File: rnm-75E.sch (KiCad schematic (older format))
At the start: 12 parts

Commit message: new crystal
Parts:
- removed C?: 1uF, symbol Device:C_Small
- removed C? (x3): 0.1uF, symbol Device:C_Small
- removed C?: 10uF, symbol Device:C_Small
- removed C? (x2): 22pF, symbol Device:C_Small
- removed R?: 10k, symbol Device:R_Small
- removed R? (x2): 22, symbol Device:R_Small
- removed U?: ATmega32U4-AU, Package_QFP:TQFP-44_10x10mm_P0.8mm, symbol MCU_Microchip_ATmega:ATmega32U4-AU
- removed Y?: 16MHz, symbol Device:Crystal_GND24_Small
- added C?: 1uF, symbol Device:C_Small
- added C? (x3): 0.1uF, symbol Device:C_Small
- added C?: 10uF, symbol Device:C_Small
- added C? (x2): 22pF, symbol Device:C_Small
- added R?: 10k, symbol Device:R_Small
- added U?: ATmega32U4-AU, Package_QFP:TQFP-44_10x10mm_P0.8mm, symbol MCU_Microchip_ATmega:ATmega32U4-AU
- added Y?: MHz, symbol Device:Crystal_GND24_Small
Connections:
- wire segments 37 -> 38

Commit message: mcu complete?
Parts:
- added R?: 10k, symbol Device:R_Small
- added R? (x2): 22k, symbol Device:R_Small
- added SW?: SW_Push, symbol Switch:SW_Push
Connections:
- net +5V: now also R?.1
- net GND: now also SW?.1
- net at U?.13 (~RESET): now also R?.2, SW?.2
- net at U?.3 (D-): now also R?.1
- net at U?.4 (D+): now also R?.1
- new net D+: R?.2
- new net D-: R?.2
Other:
- moved on the sheet: R?
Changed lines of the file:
@@
 L Device:R_Small R?
 U 1 1 609AD2BE
-P 4750 3600
-F 0 "R?" V 4554 3600 50  0000 C CNN
-F 1 "10k" V 4645 3600 50  0000 C CNN
-F 2 "" H 4750 3600 50  0001 C CNN
-F 3 "~" H 4750 3600 50  0001 C CNN
-	1    4750 3600
+P 4350 3600
+F 0 "R?" V 4154 3600 50  0000 C CNN
+F 1 "10k" V 4245 3600 50  0000 C CNN
+F 2 "" H 4350 3600 50  0001 C CNN
+F 3 "~" H 4350 3600 50  0001 C CNN
+	1    4350 3600
 	0    1    1    0
 $EndComp
@@
 L power:GND #PWR?
 U 1 1 609AEDAA
-P 5250 3600
-F 0 "#PWR?" H 5250 3350 50  0001 C CNN
-F 1 "GND" H 5255 3427 50  0000 C CNN
-F 2 "" H 5250 3600 50  0001 C CNN
-F 3 "" H 5250 3600 50  0001 C CNN
-	1    5250 3600
-	1    0    0    -1
-$EndComp
-Wire Wire Line
-	4150 3600 4650 3600
-Wire Wire Line
-	4850 3600 5250 3600
+P 4650 3600
+F 0 "#PWR?" H 4650 3350 50  0001 C CNN
+F 1 "GND" H 4655 3427 50  0000 C CNN
+F 2 "" H 4650 3600 50  0001 C CNN
+F 3 "" H 4650 3600 50  0001 C CNN
+	1    4650 3600
+	1    0    0    -1
+$EndComp
+Wire Wire Line
+	4150 3600 4250 3600
 $Comp
 L Device:C_Small C?
@@
 L power:+5V #PWR?
 U 1 1 609B8BFA
-P 1250 2300
-F 0 "#PWR?" H 1250 2150 50  0001 C CNN
-F 1 "+5V" H 1265 2473 50  0000 C CNN
-F 2 "" H 1250 2300 50  0001 C CNN
-F 3 "" H 1250 2300 50  0001 C CNN
-	1    1250 2300
-	1    0    0    -1
-$EndComp
-Wire Wire Line
-	1250 2300 2950 2300
+P 2200 2300
+F 0 "#PWR?" H 2200 2150 50  0001 C CNN
+F 1 "+5V" H 2215 2473 50  0000 C CNN
+F 2 "" H 2200 2300 50  0001 C CNN
+F 3 "" H 2200 2300 50  0001 C CNN
+	1    2200 2300
+	1    0    0    -1
+$EndComp
 $Comp
 L Device:Crystal_GND24_Small Y?
@@
 Wire Wire Line
 	2100 2000 2100 1800
+$Comp
+L Switch:SW_Push SW?
+U 1 1 609C5DAF
+P 2500 1500
+F 0 "SW?" H 2500 1785 50  0000 C CNN
+F 1 "SW_Push" H 2500 1694 50  0000 C CNN
+F 2 "" H 2500 1700 50  0001 C CNN
+F 3 "~" H 2500 1700 50  0001 C CNN
+	1    2500 1500
+	1    0    0    -1
+$EndComp
+$Comp
+L power:GND #PWR?
+U 1 1 609C76B8
+P 1700 1350
+F 0 "#PWR?" H 1700 1100 50  0001 C CNN
+F 1 "GND" H 1705 1177 50  0000 C CNN
+F 2 "" H 1700 1350 50  0001 C CNN
+F 3 "" H 1700 1350 50  0001 C CNN
+	1    1700 1350
+	1    0    0    -1
+$EndComp
+Wire Wire Line
+	1700 1350 1700 1250
+Wire Wire Line
+	1700 1250 2150 1250
+Wire Wire Line
+	2150 1250 2150 1500
+Wire Wire Line
+	2150 1500 2300 1500
+Wire Wire Line
+	2700 1500 2800 1500
+$Comp
+L Device:R_Small R?
+U 1 1 609CB514
+P 2800 1300
+F 0 "R?" H 2859 1346 50  0000 L CNN
+F 1 "10k" H 2859 1255 50  0000 L CNN
+F 2 "" H 2800 1300 50  0001 C CNN
+F 3 "~" H 2800 1300 50  0001 C CNN
+	1    2800 1300
+	1    0    0    -1
+$EndComp
+$Comp
+L power:+5V #PWR?
+U 1 1 609CC955
+P 2800 1100
+F 0 "#PWR?" H 2800 950 50  0001 C CNN
+F 1 "+5V" H 2815 1273 50  0000 C CNN
+F 2 "" H 2800 1100 50  0001 C CNN
+F 3 "" H 2800 1100 50  0001 C CNN
+	1    2800 1100
+	1    0    0    -1
+$EndComp
+Connection ~ 2800 1500
+Wire Wire Line
+	2800 1500 2950 1500
+Wire Wire Line
+	2800 1400 2800 1500
+Wire Wire Line
+	2800 1200 2800 1100
+Text GLabel 1400 2500 0    50   Input ~ 0
+D+
+Text GLabel 1400 2600 0    50   Input ~ 0
+D-
+Wire Wire Line
+	2950 2500 1850 2500
+$Comp
+L Device:R_Small R?
+U 1 1 609D1BD5
+P 1750 2500
+F 0 "R?" V 1554 2500 50  0000 C CNN
+F 1 "22k" V 1645 2500 50  0000 C CNN
+F 2 "" H 1750 2500 50  0001 C CNN
+F 3 "~" H 1750 2500 50  0001 C CNN
+	1    1750 2500
+	0    1    1    0
+$EndComp
+Wire Wire Line
+	1650 2500 1400 2500
+Wire Wire Line
+	1400 2600 1900 2600
+$Comp
+L Device:R_Small R?
+U 1 1 609D369C
+P 2000 2600
+F 0 "R?" V 1804 2600 50  0000 C CNN
+F 1 "22k" V 1895 2600 50  0000 C CNN
+F 2 "" H 2000 2600 50  0001 C CNN
+F 3 "~" H 2000 2600 50  0001 C CNN
+	1    2000 2600
+	0    1    1    0
+$EndComp
+Wire Wire Line
+	2100 2600 2950 2600
+Wire Wire Line
+	2200 2300 2950 2300
+Wire Wire Line
+	4450 3600 4650 3600
 $EndSCHEMATC

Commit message: ref made
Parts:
- added D1, D2, D3, D4: D_Small, Diode_SMD:D_SOD-123, symbol Device:D_Small
- added F1: Polyfuse, Fuse:Fuse_1206_3216Metric, symbol Device:Polyfuse
- added MX1, MX2, MX3, MX4: MX-NoLED, MX_ALPS:MX-1U-NoLED, symbol MX_ALPS:MX-NoLED
- added USB1: Molex-0548190519, random_keyboard_parts:Molex-0548190589, symbol random_keyb_parts:Molex-0548190519
- C1, C2, C3, C4, C5, C6: renamed from C?; footprint (none) -> Capacitor_SMD:C_0805_2012Metric
- C7: renamed from C?; footprint (none) -> Diode_SMD:D_SOD-123
- R1, R2, R3, R4: renamed from R?; footprint (none) -> Resistor_SMD:R_0805_2012Metric
- SW1: renamed from SW?; footprint (none) -> random_keyboard_parts:SKQG-1155865
- Y1: renamed from Y?; footprint (none) -> Package_QFP:TQFP-44_10x10mm_P0.8mm
- gave numbers to parts that had none: 1
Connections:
- net +5V: now also F1.1
- net D+: now also USB1.3 (D+)
- net D-: now also USB1.4 (D-)
- net GND: now also USB1.1 (GND)
- net ROW0: now reaches U1.27 (PD7)
- net ROW0: now also D1.1 (K), D3.1 (K)
- net COL1: now reaches U1.28 (PB4)
- net COL1: now also MX3.1 (COL), MX4.1 (COL)
- net COL0: now reaches U1.29 (PB5)
- net COL0: now also MX1.1 (COL), MX2.1 (COL)
- net ROW1: now reaches U1.30 (PB6)
- net ROW1: now also D2.1 (K), D4.1 (K)
- new net: D1.2 (A), MX1.2 (ROW)
- new net: D3.2 (A), MX3.2 (ROW)
- new net: D2.2 (A), MX2.2 (ROW)
- new net: D4.2 (A), MX4.2 (ROW)
- new net VCC: F1.2, USB1.5 (VBUS)
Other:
- moved on the sheet: R4

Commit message: added ground fill
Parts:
- added C8: 0.1uF, Capacitor_SMD:C_0805_2012Metric, symbol Device:C_Small
- Y1: value MHz -> Crystal_GND24_Small; footprint Package_QFP:TQFP-44_10x10mm_P0.8mm -> Crystal:Crystal_SMD_3225-4Pin_3.2x2.5mm
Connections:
- net +5V: now also C8.1
- net GND: now also C8.2
- net ROW1: now also U1.26 (PD6); no longer U1.30 (PB6)
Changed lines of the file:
@@
 $EndComp
-$Comp
-L Device:Crystal_GND24_Small Y1
-U 1 1 609BC559
-P 2250 1800
-F 0 "Y1" V 2204 1944 50  0000 L CNN
-F 1 "MHz" V 2295 1944 50  0000 L CNN
-F 2 "Package_QFP:TQFP-44_10x10mm_P0.8mm" H 2250 1800 50  0001 C CNN
-F 3 "~" H 2250 1800 50  0001 C CNN
-	1    2250 1800
-	0    1    1    0
-$EndComp
-Wire Wire Line
-	2250 1700 2950 1700
-Wire Wire Line
-	2950 1900 2250 1900
 $Comp
 L Device:C_Small C4
@@
 	2050 1950 2050 1900
 Wire Wire Line
-	2050 1900 2250 1900
-Connection ~ 2250 1900
-Wire Wire Line
 	2050 1600 2050 1700
-Wire Wire Line
-	2050 1700 2250 1700
-Connection ~ 2250 1700
 Wire Wire Line
 	1850 1600 1850 1950
@@
 Wire Wire Line
 	4150 3600 4400 3600
-Text GLabel 4150 2100 2    50   Input ~ 0
+Text GLabel 4150 3300 2    50   Input ~ 0
 ROW1
 Text GLabel 4150 2000 2    50   Input ~ 0
@@
 Text GLabel 4150 1900 2    50   Input ~ 0
 COL1
+$Comp
+L Device:Crystal_GND24_Small Y1
+U 1 1 609B4FA0
+P 2250 1800
+F 0 "Y1" V 2204 1944 50  0000 L CNN
+F 1 "Crystal_GND24_Small" V 2295 1944 50  0000 L CNN
+F 2 "Crystal:Crystal_SMD_3225-4Pin_3.2x2.5mm" H 2250 1800 50  0001 C CNN
+F 3 "~" H 2250 1800 50  0001 C CNN
+	1    2250 1800
+	0    1    1    0
+$EndComp
+Wire Wire Line
+	2050 1700 2250 1700
+Wire Wire Line
+	2050 1900 2250 1900
+Connection ~ 2250 1700
+Wire Wire Line
+	2250 1700 2950 1700
+Connection ~ 2250 1900
+Wire Wire Line
+	2250 1900 2950 1900
+$Comp
+L Device:C_Small C8
+U 1 1 60A5117E
+P 550 4200
+F 0 "C8" H 642 4246 50  0000 L CNN
+F 1 "0.1uF" H 642 4155 50  0000 L CNN
+F 2 "Capacitor_SMD:C_0805_2012Metric" H 550 4200 50  0001 C CNN
+F 3 "~" H 550 4200 50  0001 C CNN
+	1    550  4200
+	1    0    0    -1
+$EndComp
+Wire Wire Line
+	550  4300 850  4300
+Connection ~ 850  4300
+Wire Wire Line
+	850  4100 550  4100
+Connection ~ 850  4100
 $EndSCHEMATC

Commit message: keyboard schematic done
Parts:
- removed C1, C2, C3, C8: 0.1uF, Capacitor_SMD:C_0805_2012Metric, symbol Device:C_Small
- removed C4, C5: 22pF, Capacitor_SMD:C_0805_2012Metric, symbol Device:C_Small
- removed C6: 10uF, Capacitor_SMD:C_0805_2012Metric, symbol Device:C_Small
- removed C7: 1uF, Diode_SMD:D_SOD-123, symbol Device:C_Small
- removed D1, D2, D3, D4: D_Small, Diode_SMD:D_SOD-123, symbol Device:D_Small
- removed F1: Polyfuse, Fuse:Fuse_1206_3216Metric, symbol Device:Polyfuse
- removed MX1, MX2, MX3, MX4: MX-NoLED, MX_ALPS:MX-1U-NoLED, symbol MX_ALPS:MX-NoLED
- removed R1, R2: 22k, Resistor_SMD:R_0805_2012Metric, symbol Device:R_Small
- removed R3, R4: 10k, Resistor_SMD:R_0805_2012Metric, symbol Device:R_Small
- removed SW1: SW_Push, random_keyboard_parts:SKQG-1155865, symbol Switch:SW_Push
- removed U1: ATmega32U4-AU, Package_QFP:TQFP-44_10x10mm_P0.8mm, symbol MCU_Microchip_ATmega:ATmega32U4-AU
- removed USB1: Molex-0548190519, random_keyboard_parts:Molex-0548190589, symbol random_keyb_parts:Molex-0548190519
- removed Y1: Crystal_GND24_Small, Crystal:Crystal_SMD_3225-4Pin_3.2x2.5mm, symbol Device:Crystal_GND24_Small
- added CF3, C_F1, C_F2, C_F4: 0.1uF, symbol Device:C_Small
- added C_FM: 10uF, symbol Device:C_Small
- added C_X1, C_X2: 22pF, symbol Device:C_Small
- added C_ucap: 1uF, symbol Device:C_Small
- added D? (x87): D_Small, symbol Device:D_Small
- added ESD?: PRTR5V0U2X, Package_TO_SOT_SMD:SOT-143, symbol Power_Protection:PRTR5V0U2X
- added F1: 500mA, symbol Device:Polyfuse_Small
- added J?: USB_C_Receptacle_USB2.0, symbol Connector:USB_C_Receptacle_USB2.0
- added J?: AVR-ISP-6, symbol Connector:AVR-ISP-6
- added MX? (x89): MX-NoLED, symbol MX_ALPS_HYBRID:MX-NoLED
- added R_SW1, R_SW2: 10k, symbol Device:R_Small
- added R_d1, R_d2: 22, symbol Device:R_Small
- added R_u1, R_u2: 5.1k, symbol Device:R_Small
- added SW?: SW_Push, symbol Switch:SW_Push
- added U?: ATmega32U4-AU, Package_QFP:TQFP-44_10x10mm_P0.8mm, symbol MCU_Microchip_ATmega:ATmega32U4-AU
- added Y?: Crystal_GND24_Small, symbol Device:Crystal_GND24_Small
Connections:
- net +5V: now also CF3.1, C_F1.1, C_F2.1, C_F4.1, C_FM.1, ESD?.4 (VCC), F1.1, R_SW1.2, U?.14 (VCC), U?.2 (UVCC), U?.24 (AVCC), U?.34 (VCC), U?.44 (AVCC), U?.7 (VBUS)
- net COL0: now also MX?.1 (COL), MX?.1 (COL), MX?.1 (COL), MX?.1 (COL), MX?.1 (COL)
- net COL1: now also MX?.1 (COL), MX?.1 (COL), MX?.1 (COL), MX?.1 (COL), MX?.1 (COL), MX?.1 (COL)
- net D+: now also ESD?.3 (I/O2), R_d1.1, U?.4 (D+)
- net D-: now also ESD?.2 (I/O1), R_d2.1, U?.3 (D-)
- net GND: now also CF3.2, C_F1.2, C_F2.2, C_F4.2, C_FM.2, C_X1.1, C_X2.1, C_ucap.1, ESD?.1 (GND), J?.6 (GND), J?.A1 (GND), J?.A12 (GND), J?.B1 (GND), J?.B12 (GND), J?.S1 (SHIELD), R_SW2.1, R_u1.1, R_u2.1, SW?.1, U?.15 (GND), U?.23 (GND), U?.35 (GND), U?.43 (GND), U?.5 (UGND), Y?.2, Y?.4
- net VCC: now also F1.2, J?.2 (VCC), J?.A4 (VBUS), J?.A9 (VBUS), J?.B4 (VBUS), J?.B9 (VBUS)
- new net: J?.A5 (CC1), R_u1.2
- new net: J?.B5 (CC2), R_u2.2
- new net: R_SW2.2, U?.33 (~HWB~/PE2)
- new net: C_ucap.2, U?.6 (UCAP)
- new net: D?.2 (A), MX?.2 (ROW) (x85)
- new net: D?.2 (A), MX?.2 (ROW), MX?.2 (ROW) (x2)
- new net COL10: MX?.1 (COL), MX?.1 (COL), MX?.1 (COL), MX?.1 (COL), MX?.1 (COL), MX?.1 (COL), MX?.1 (COL)
- new net COL11: MX?.1 (COL), MX?.1 (COL), MX?.1 (COL), MX?.1 (COL), MX?.1 (COL), MX?.1 (COL), MX?.1 (COL)
- new net COL12: MX?.1 (COL), MX?.1 (COL), MX?.1 (COL), MX?.1 (COL), MX?.1 (COL), MX?.1 (COL)
- new net COL13: MX?.1 (COL), MX?.1 (COL), MX?.1 (COL)
- new net COL14: MX?.1 (COL), MX?.1 (COL), MX?.1 (COL), MX?.1 (COL), MX?.1 (COL), MX?.1 (COL)
- new net COL15: MX?.1 (COL), MX?.1 (COL), MX?.1 (COL), MX?.1 (COL), MX?.1 (COL)
- new net COL2: MX?.1 (COL), MX?.1 (COL), MX?.1 (COL), MX?.1 (COL), MX?.1 (COL), MX?.1 (COL)
- new net COL3: MX?.1 (COL), MX?.1 (COL), MX?.1 (COL), MX?.1 (COL), MX?.1 (COL), MX?.1 (COL)
- new net COL4: MX?.1 (COL), MX?.1 (COL), MX?.1 (COL), MX?.1 (COL), MX?.1 (COL)
- new net COL5: MX?.1 (COL), MX?.1 (COL), MX?.1 (COL), MX?.1 (COL), MX?.1 (COL)
- new net COL6: MX?.1 (COL), MX?.1 (COL), MX?.1 (COL), MX?.1 (COL), MX?.1 (COL), MX?.1 (COL)
- new net COL7: MX?.1 (COL), MX?.1 (COL), MX?.1 (COL), MX?.1 (COL), MX?.1 (COL)
- new net COL8: MX?.1 (COL), MX?.1 (COL), MX?.1 (COL), MX?.1 (COL), MX?.1 (COL)
- new net COL9: MX?.1 (COL), MX?.1 (COL), MX?.1 (COL), MX?.1 (COL), MX?.1 (COL), MX?.1 (COL)
- new net D+1: J?.A6 (D+), J?.B6 (D+), R_d1.2
- new net D-1: J?.A7 (D-), J?.B7 (D-), R_d2.2
- new net MISO: J?.1 (MISO), U?.8 (PB0)
- new net MOSI: J?.4 (MOSI), U?.9 (PB1)
- new net RESET: J?.5 (~RST), R_SW1.1, SW?.2, U?.13 (~RESET)
- new net ROWA: D?.1 (K), D?.1 (K), D?.1 (K), D?.1 (K), D?.1 (K), D?.1 (K), D?.1 (K), D?.1 (K), D?.1 (K), D?.1 (K), D?.1 (K), D?.1 (K), D?.1 (K), D?.1 (K)
- new net ROWB: D?.1 (K), D?.1 (K), D?.1 (K), D?.1 (K), D?.1 (K), D?.1 (K), D?.1 (K), D?.1 (K), D?.1 (K), D?.1 (K), D?.1 (K), D?.1 (K), D?.1 (K), D?.1 (K), D?.1 (K), D?.1 (K)
- new net ROWC: D?.1 (K), D?.1 (K), D?.1 (K), D?.1 (K), D?.1 (K), D?.1 (K), D?.1 (K), D?.1 (K), D?.1 (K), D?.1 (K), D?.1 (K), D?.1 (K), D?.1 (K), D?.1 (K), D?.1 (K), D?.1 (K)
- new net ROWD: D?.1 (K), D?.1 (K), D?.1 (K), D?.1 (K), D?.1 (K), D?.1 (K), D?.1 (K), D?.1 (K), D?.1 (K), D?.1 (K), D?.1 (K), D?.1 (K), D?.1 (K), D?.1 (K), D?.1 (K)
- new net ROWE: D?.1 (K), D?.1 (K), D?.1 (K), D?.1 (K), D?.1 (K), D?.1 (K), D?.1 (K), D?.1 (K), D?.1 (K), D?.1 (K), D?.1 (K), D?.1 (K), D?.1 (K), D?.1 (K), D?.1 (K)
- new net ROWF: D?.1 (K), D?.1 (K), D?.1 (K), D?.1 (K), D?.1 (K), D?.1 (K), D?.1 (K), D?.1 (K), D?.1 (K), D?.1 (K), D?.1 (K)
- new net SCK: J?.3 (SCK), U?.12 (PB7)
- new net XTAL1: C_X1.2, U?.17 (XTAL1), Y?.1
- new net XTAL2: C_X2.2, U?.16 (XTAL2), Y?.3
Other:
- note added: "ARROW CLUSTER"
- note added: "CAPS TO ENTER\n"
- note added: "CTRL WIN ALT SPACE ALT CTRL"
- note added: "ESC F1-12 + DEL"
- note added: "LEFT MACRO COLUMN"
- note added: "LS to RS + UP ARROW\n"
- note added: "MISO and MOSI are good on 8/9 or 10/11. 13 is RESET 12 is on another bank. 7 5v 8-11 good"
- note added: "OK. PORTS 25-32 are very nice to use. Ports 36-42 are also very nice to use. \n18-22 also very nice. Total gives 20 EZ access"
- note added: "Right macro column\n"
- note added: "TAB to \|"
- note added: "` 1-0 -+ bs"

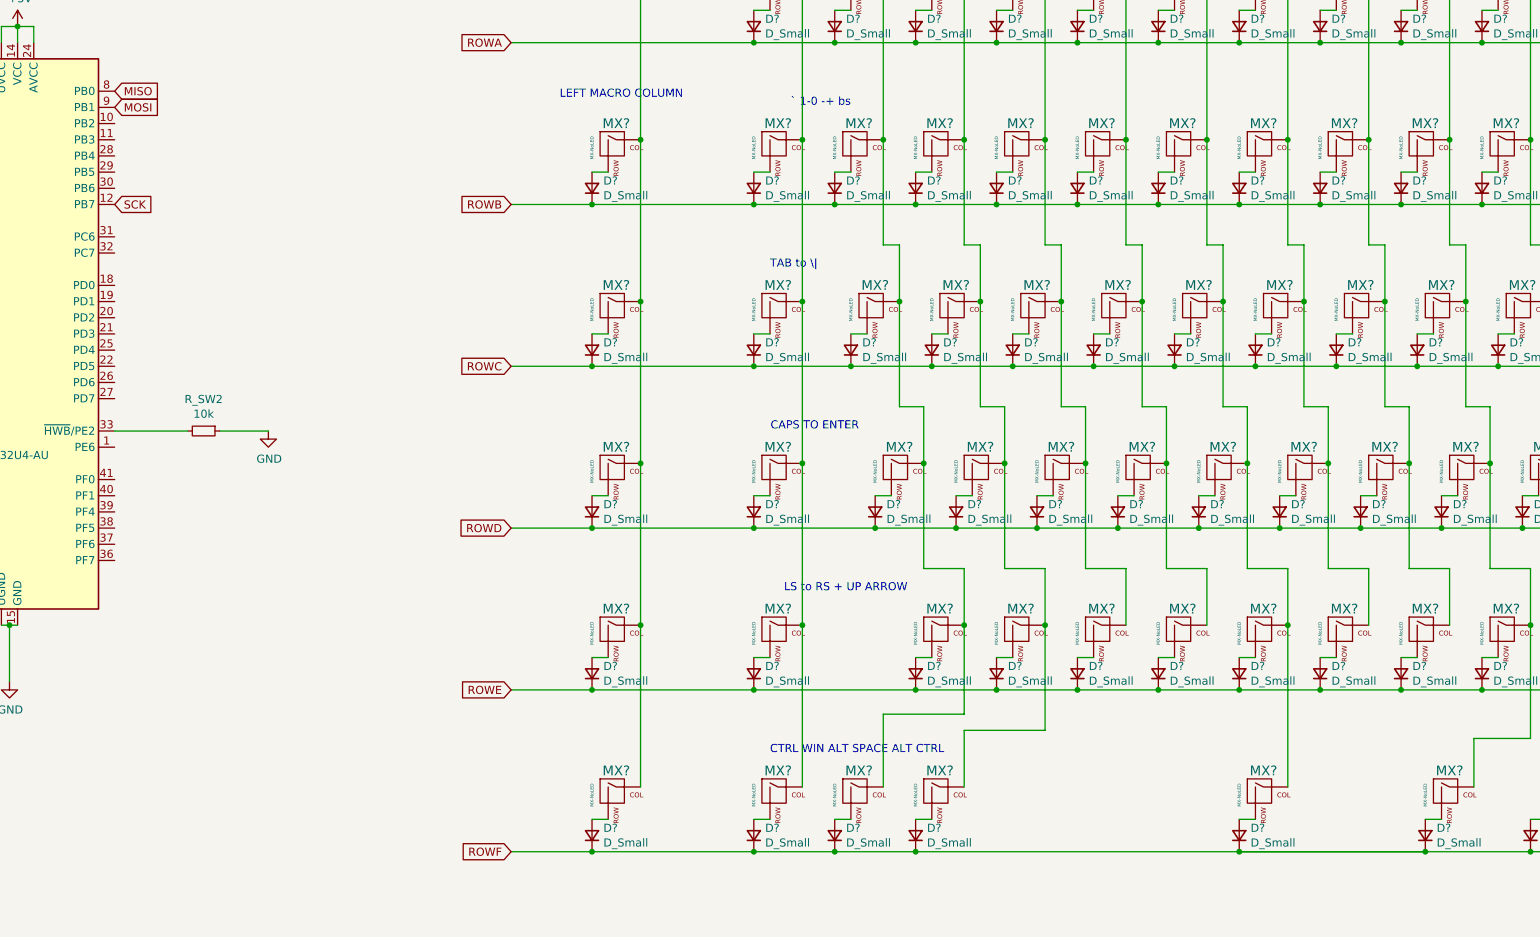
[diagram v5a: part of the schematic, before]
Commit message: wrong encoder
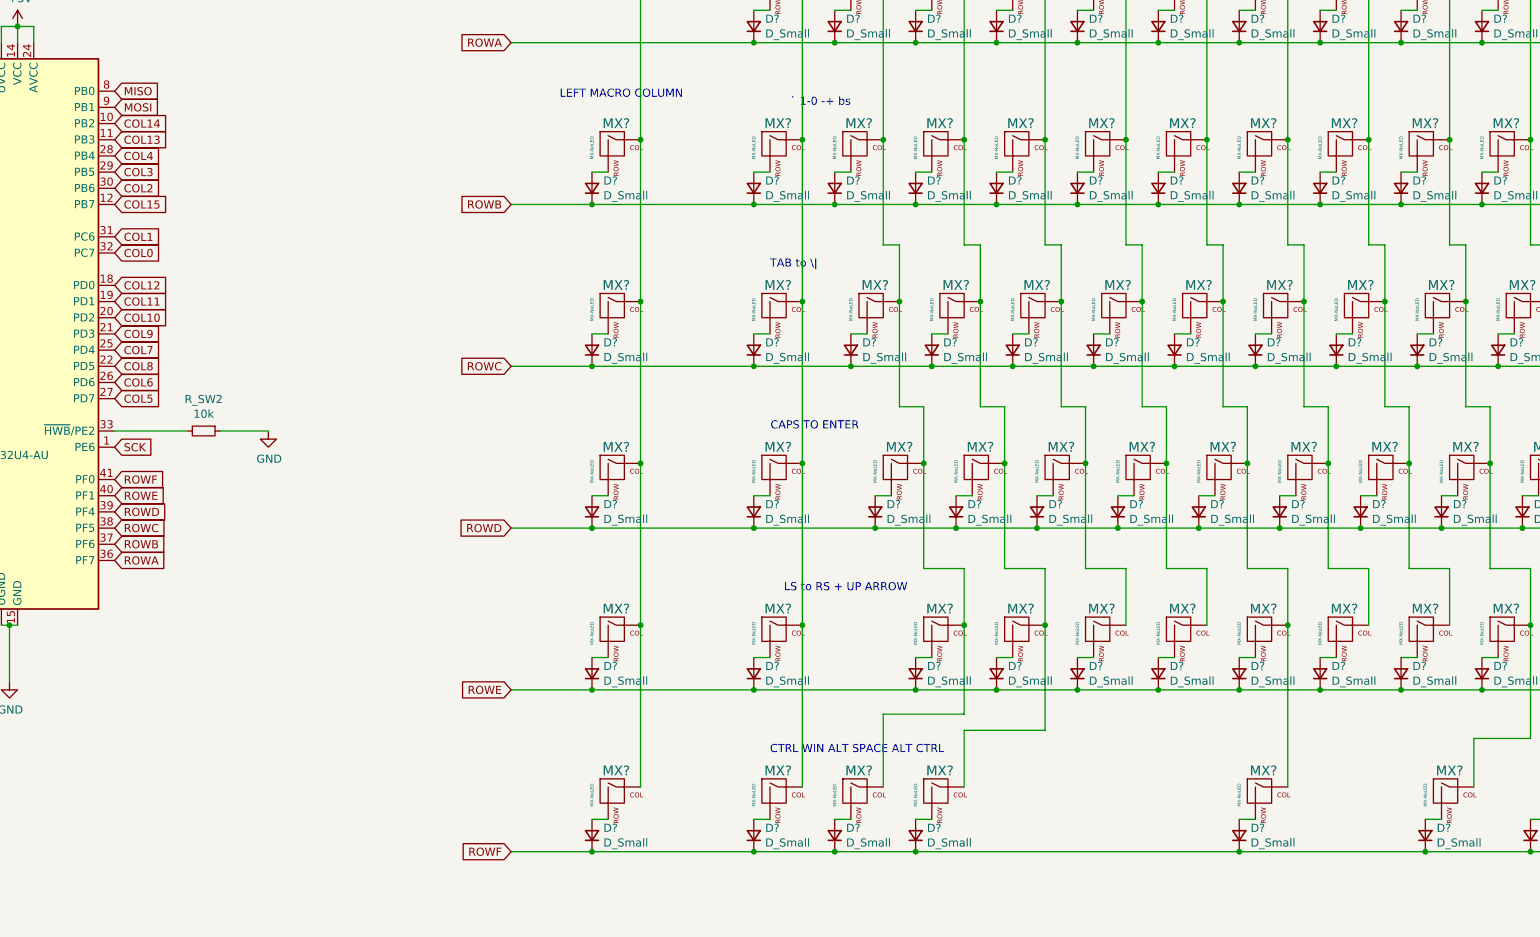
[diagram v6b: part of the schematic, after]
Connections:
- net COL0: now also U?.32 (PC7)
- net COL1: now also U?.31 (PC6)
- net COL10: now also U?.20 (PD2)
- net COL11: now also U?.19 (PD1)
- net COL12: now also U?.18 (PD0)
- net COL13: now also U?.11 (PB3)
- net COL14: now also U?.10 (PB2)
- net COL15: now also U?.12 (PB7)
- net COL2: now also U?.30 (PB6)
- net COL3: now also U?.29 (PB5)
- net COL4: now also U?.28 (PB4)
- net COL5: now also U?.27 (PD7)
- net COL6: now also U?.26 (PD6)
- net COL7: now also U?.25 (PD4)
- net COL8: now also U?.22 (PD5)
- net COL9: now also U?.21 (PD3)
- net ROWA: now also U?.36 (PF7)
- net ROWB: now also U?.37 (PF6)
- net ROWC: now also U?.38 (PF5)
- net ROWD: now also U?.39 (PF4)
- net ROWE: now also U?.40 (PF1)
- net ROWF: now also U?.41 (PF0)
- net SCK: now also U?.1 (PE6); no longer U?.12 (PB7)
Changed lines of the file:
@@
 Wire Wire Line
 	6150 3600 5950 3600
-Text GLabel 10050 2000 2    50   Input ~ 0
+Text GLabel 10050 3500 2    50   Input ~ 0
 SCK
 Text GLabel 10050 1400 2    50   Input ~ 0
@@
 Wire Wire Line
 	19450 5800 19600 5800
-Wire Wire Line
-	18150 6000 17000 6000
 Connection ~ 18150 6000
 Wire Wire Line
 	18150 6000 18800 6000
+Text GLabel 10050 3700 2    50   Input ~ 0
+ROWF
+Text GLabel 10050 3800 2    50   Input ~ 0
+ROWE
+Text GLabel 10050 3900 2    50   Input ~ 0
+ROWD
+Text GLabel 10050 4000 2    50   Input ~ 0
+ROWC
+Text GLabel 10050 4100 2    50   Input ~ 0
+ROWB
+Text GLabel 10050 4200 2    50   Input ~ 0
+ROWA
+Text GLabel 10050 2300 2    50   Input ~ 0
+COL0
+Text GLabel 10050 2200 2    50   Input ~ 0
+COL1
+Text GLabel 10050 1900 2    50   Input ~ 0
+COL2
+Text GLabel 10050 1800 2    50   Input ~ 0
+COL3
+Text GLabel 10050 1700 2    50   Input ~ 0
+COL4
+Text GLabel 10050 3200 2    50   Input ~ 0
+COL5
+Text GLabel 10050 3100 2    50   Input ~ 0
+COL6
+Text GLabel 10050 2900 2    50   Input ~ 0
+COL7
+Text GLabel 10050 3000 2    50   Input ~ 0
+COL8
+Text GLabel 10050 2800 2    50   Input ~ 0
+COL9
+Text GLabel 10050 2700 2    50   Input ~ 0
+COL10
+Text GLabel 10050 2600 2    50   Input ~ 0
+COL11
+Text GLabel 10050 2500 2    50   Input ~ 0
+COL12
+Text GLabel 10050 1600 2    50   Input ~ 0
+COL13
+Text GLabel 10050 1500 2    50   Input ~ 0
+COL14
+Text GLabel 10050 2000 2    50   Input ~ 0
+COL15
 $EndSCHEMATC
